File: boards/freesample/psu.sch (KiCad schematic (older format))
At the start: 0 parts

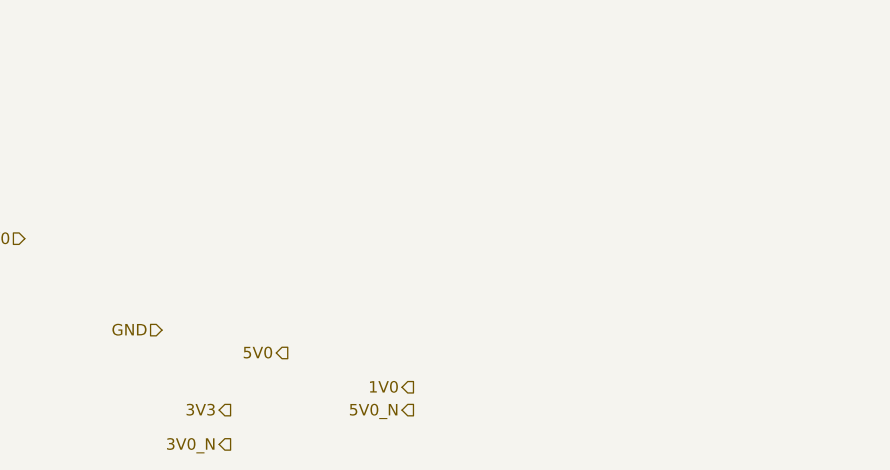
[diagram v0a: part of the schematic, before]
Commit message: Continued initial schematic capture
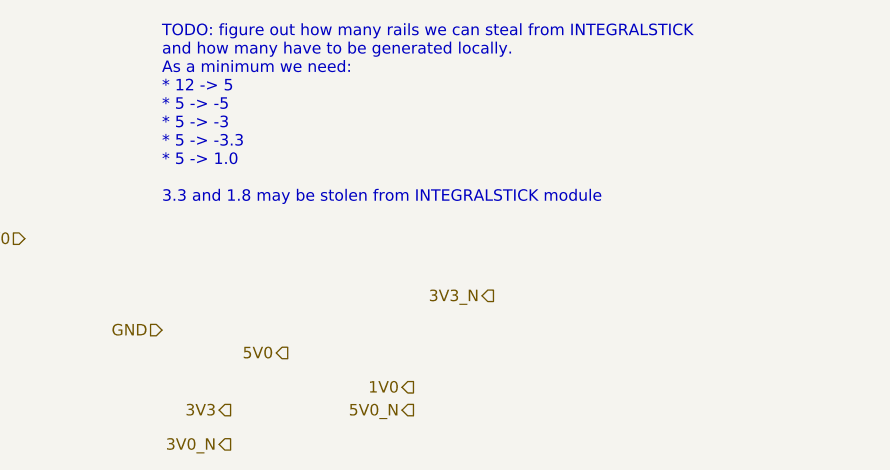
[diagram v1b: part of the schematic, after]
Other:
- note added: "TODO: figure out how many rails we can steal from INTEGRALSTICK\nand how many have to be generated locally.\nAs a minimum we need:\n* 12 -> 5\n* 5 -> -5\n* 5 -> -3\n* 5 -> -3.3\n* 5 -> 1.0\n\n3.3 and 1.8 may be stolen from INTEGRALSTICK module"
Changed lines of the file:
@@
 $Descr A4 11693 8268
 encoding utf-8
-Sheet 10 11
+Sheet 10 12
 Title "FREESAMPLE Oscilloscope"
-Date "2018-12-15"
+Date "2018-12-17"
 Rev "0.1"
 Comp "Andrew D. Zonenberg / Antikernel Labs"
@@
 Text HLabel 1100 1750 0    50   Input ~ 0
 12V0
+Text Notes 1700 1600 0    50   ~ 0
+TODO: figure out how many rails we can steal from INTEGRALSTICK\nand how many have to be generated locally.\nAs a minimum we need:\n* 12 -> 5\n* 5 -> -5\n* 5 -> -3\n* 5 -> -3.3\n* 5 -> 1.0\n\n3.3 and 1.8 may be stolen from INTEGRALSTICK module
+Text HLabel 3150 2000 0    50   Output ~ 0
+3V3_N
 $EndSCHEMATC

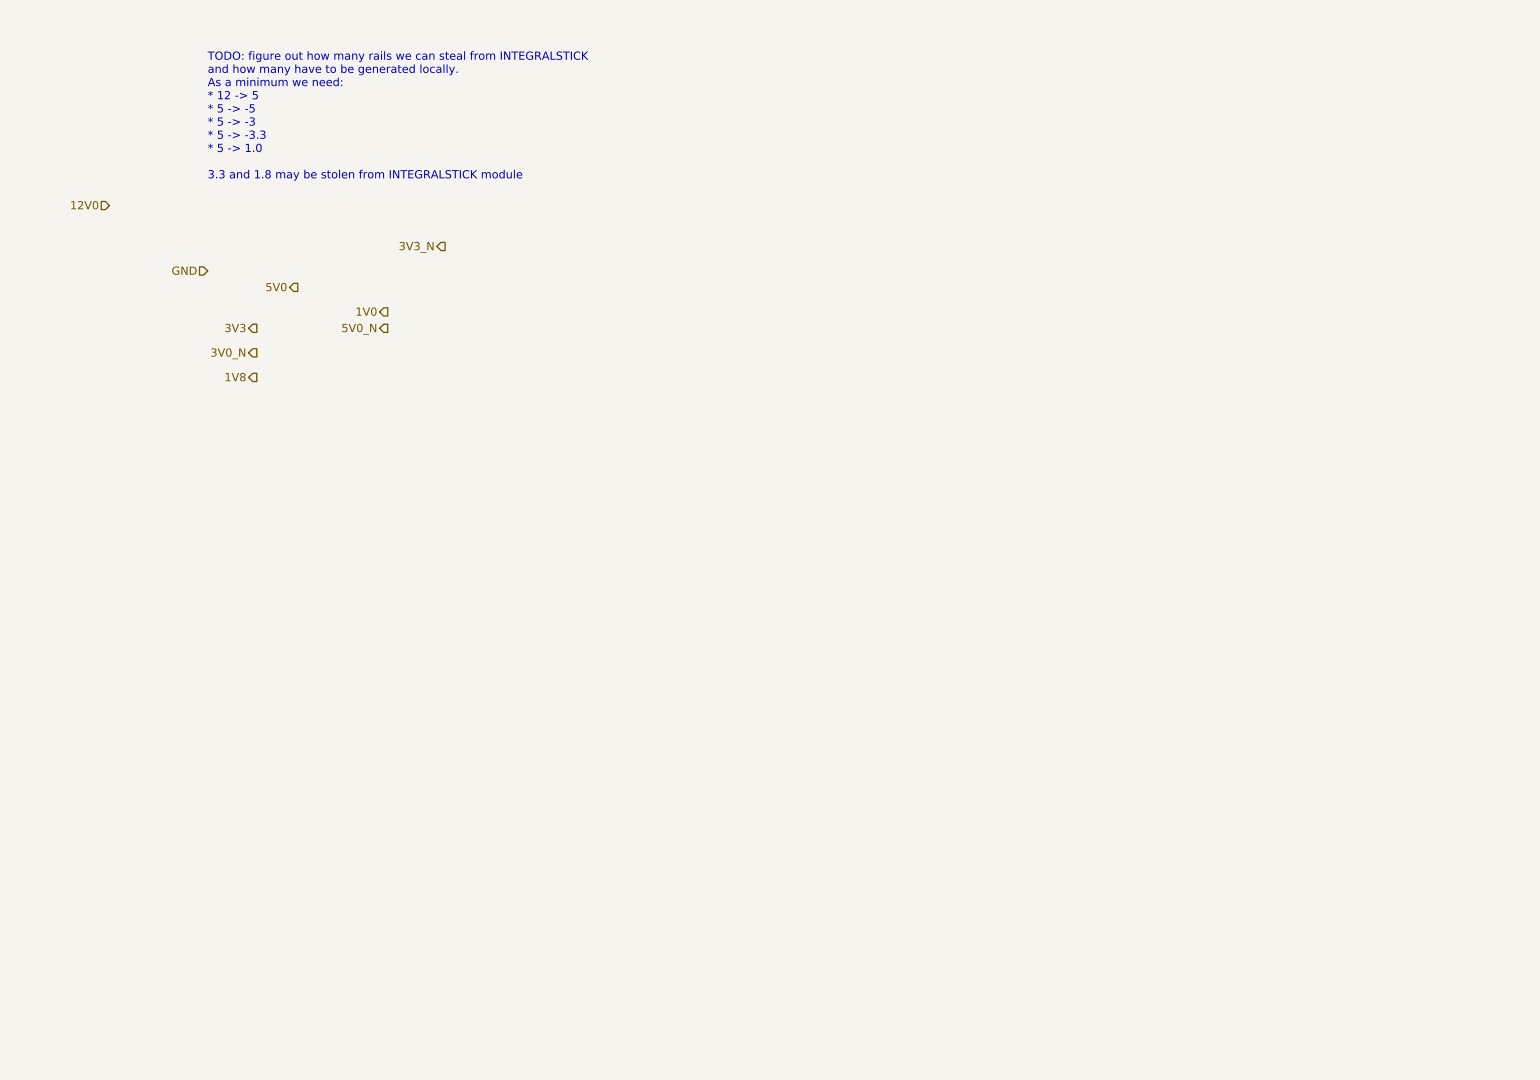
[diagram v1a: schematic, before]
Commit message: Continued work on FREESAMPLE schematic including PSU.
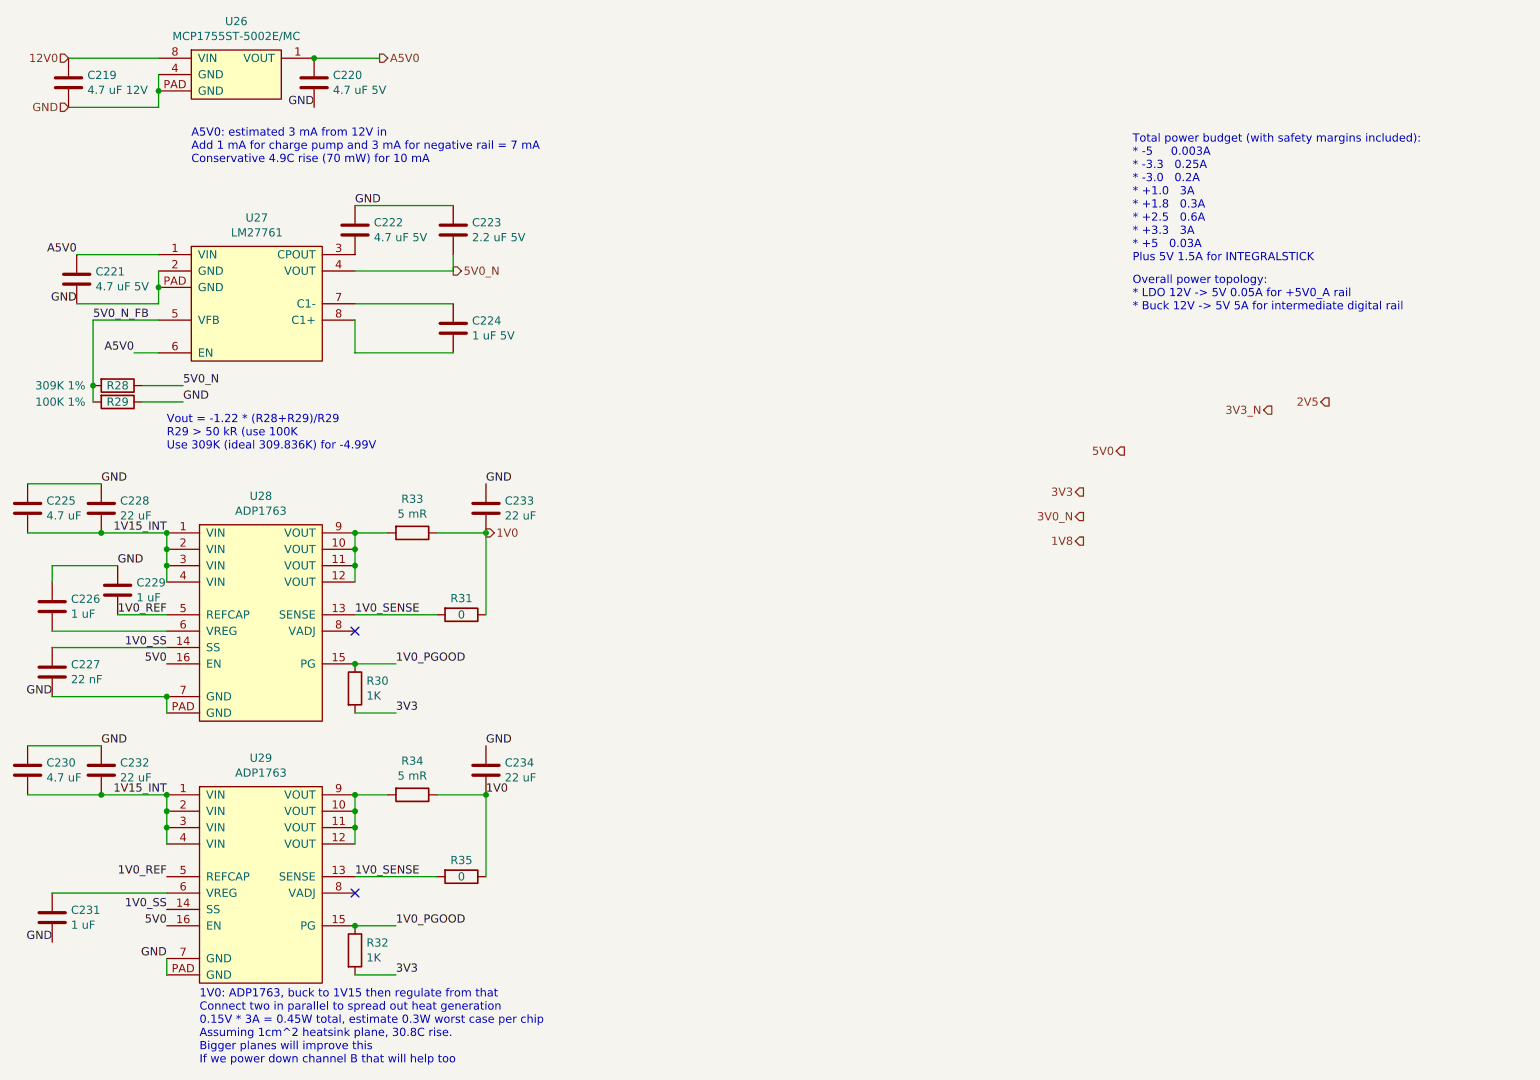
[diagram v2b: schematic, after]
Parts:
- added C219: 4.7 uF 12V, symbol device:C
- added C220, C221, C222: 4.7 uF 5V, symbol device:C
- added C223: 2.2 uF 5V, symbol device:C
- added C224: 1 uF 5V, symbol device:C
- added C225, C230: 4.7 uF, symbol device:C
- added C226, C229, C231: 1 uF, symbol device:C
- added C227: 22 nF, symbol device:C
- added C228, C232, C233, C234: 22 uF, symbol device:C
- added R28: 309K 1%, symbol device:R
- added R29: 100K 1%, symbol device:R
- added R30, R32: 1K, symbol device:R
- added R31, R35: 0, symbol device:R
- added R33, R34: 5 mR, symbol device:R
- added U26: MCP1755ST-5002E/MC, symbol power-azonenberg:MCP1755S-DFN
- added U27: LM27761, symbol power-azonenberg:LM27761
- added U28, U29: ADP1763, symbol power-azonenberg:ADP1763
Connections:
- net 12V0: now also C219.1, U26.8 (VIN)
- net 1V0: now also C233.1, C234.1, R31.1, R33.1, R34.1, R35.1
- net 3V3: now also R30.2, R32.2
- net 5V0: now also U28.16 (EN), U29.16 (EN)
- net 5V0_N: now also C223.2, R28.1, U27.4 (VOUT)
- net GND: now also C219.2, C220.2, C221.2, C222.1, C223.1, C225.2, C226.2, C227.1, C228.2, C229.2, C230.2, C231.1, C232.2, C233.2, C234.2, R29.1, U26.4 (GND), U26.PAD (GND), U27.2 (GND), U27.PAD (GND), U28.7 (GND), U28.PAD (GND), U29.7 (GND), U29.PAD (GND)
- new net: C222.2, U27.3 (CPOUT)
- new net: C224.1, U27.7 (C1-)
- new net: C224.2, U27.8 (C1+)
- new net: R33.2, U28.10 (VOUT), U28.11 (VOUT), U28.12 (VOUT), U28.9 (VOUT)
- new net: C226.1, U28.6 (VREG)
- new net: R34.2, U29.10 (VOUT), U29.11 (VOUT), U29.12 (VOUT), U29.9 (VOUT)
- new net: C231.2, U29.6 (VREG)
- new net 1V0_PGOOD: R30.1, R32.1, U28.15 (PG), U29.15 (PG)
- new net 1V0_REF: C229.1, U28.5 (REFCAP), U29.5 (REFCAP)
- new net 1V0_SENSE: R31.2, R35.2, U28.13 (SENSE), U29.13 (SENSE)
- new net 1V0_SS: C227.2, U28.14 (SS), U29.14 (SS)
- new net 1V15_INT: C225.1, C228.1, C230.1, C232.1, U28.1 (VIN), U28.2 (VIN), U28.3 (VIN), U28.4 (VIN), U29.1 (VIN), U29.2 (VIN), U29.3 (VIN), U29.4 (VIN)
- new net 5V0_N_FB: R28.2, R29.2, U27.5 (VFB)
- new net A5V0: C220.1, C221.1, U26.1 (VOUT), U27.1 (VIN), U27.6 (EN)
- no-connect marks 0 -> 2
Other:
- note added: "1V0: ADP1763, buck to 1V15 then regulate from that\nConnect two in parallel to spread out heat generation\n0.15V * 3A = 0.45W total, estimate 0.3W worst case per chip\nAssuming 1cm^2 heatsink plane, 30.8C rise.\nBigger planes will improve this\nIf we power down channel B that will help too"
- note added: "A5V0: estimated 3 mA from 12V in\nAdd 1 mA for charge pump and 3 mA for negative rail = 7 mA\nConservative 4.9C rise (70 mW) for 10 mA"
- note added: "Overall power topology:\n* LDO 12V -> 5V 0.05A for +5V0_A rail\n* Buck 12V -> 5V 5A for intermediate digital rail"
- note added: "Total power budget (with safety margins included):\n* -5 0.003A\n* -3.3 0.25A\n* -3.0 0.2A\n* +1.0 3A\n* +1.8 0.3A\n* +2.5 0.6A\n* +3.3 3A\n* +5 0.03A\nPlus 5V 1.5A for INTEGRALSTICK"
- note added: "Vout = -1.22 * (R28+R29)/R29\nR29 > 50 kR (use 100K\nUse 309K (ideal 309.836K) for -4.99V"
- note removed: "TODO: figure out how many rails we can steal from INTEGRALSTICK\nand how many have to be generated locally.\nAs a minimum we need:\n* 12 -> 5\n* 5 -> -5\n* 5 -> -3\n* 5 -> -3.3\n* 5 -> 1.0\n\n3.3 and 1.8 may be stolen from INTEGRALSTICK module"

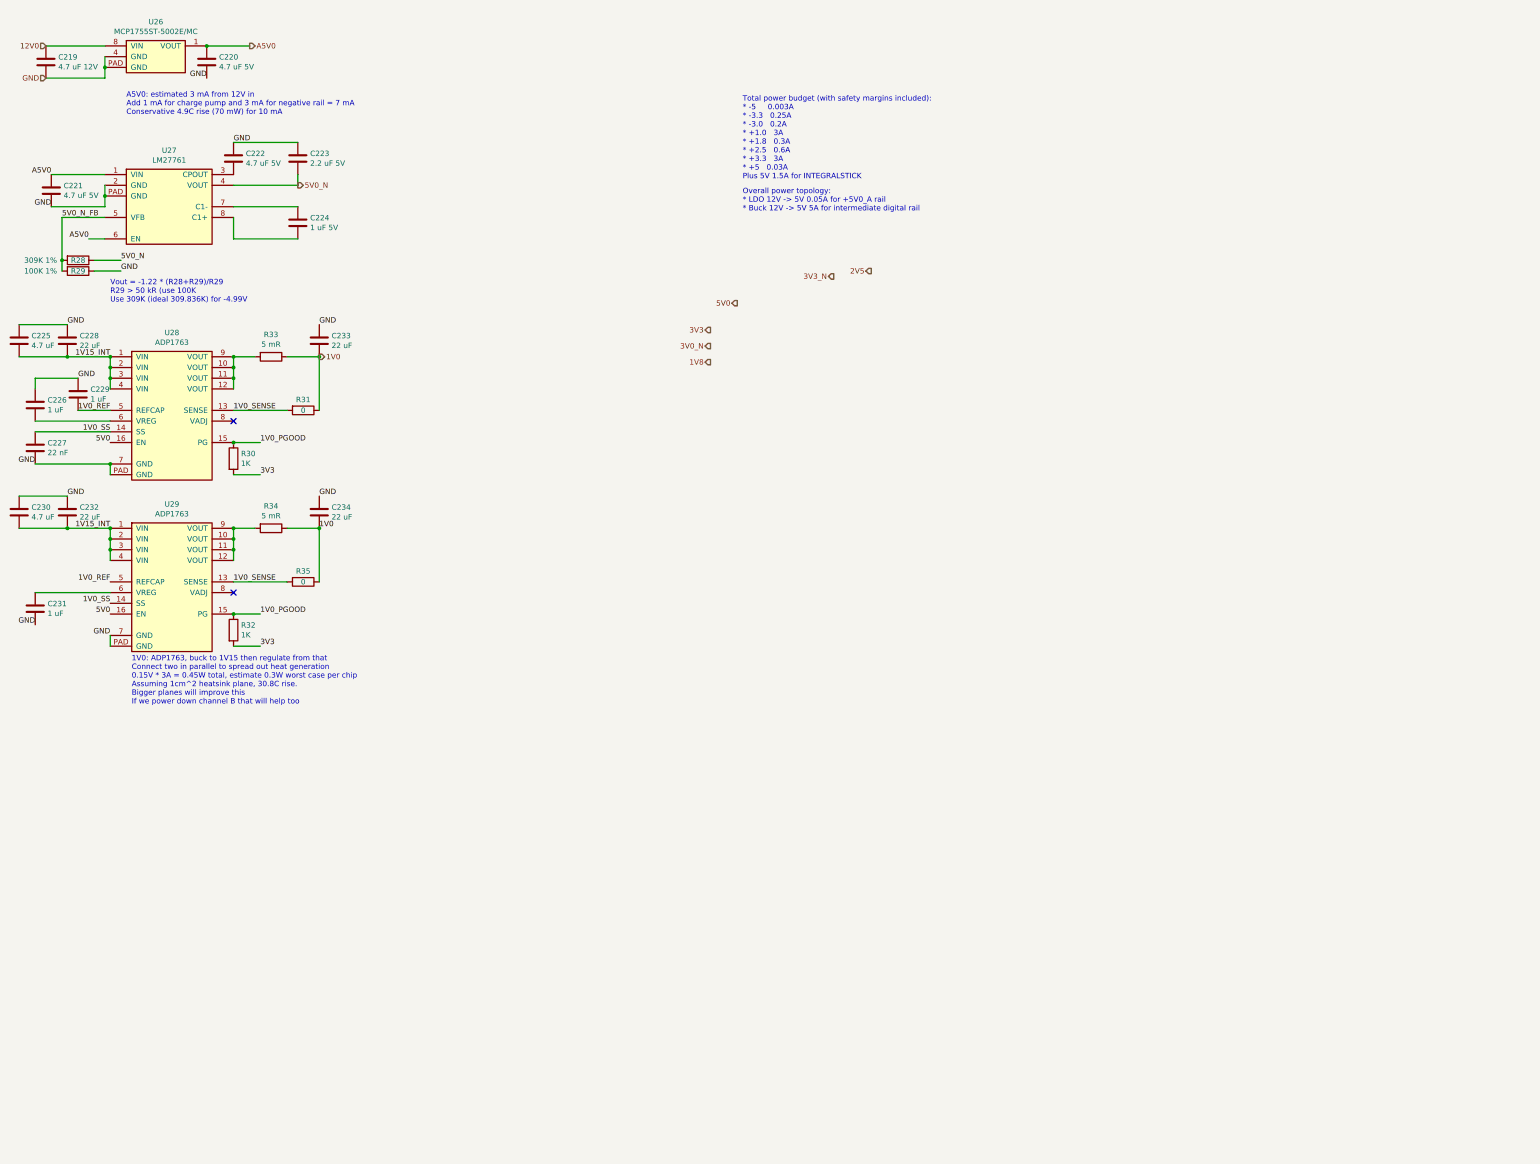
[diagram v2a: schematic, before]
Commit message: Lots more work on PSU and sch readability improvements
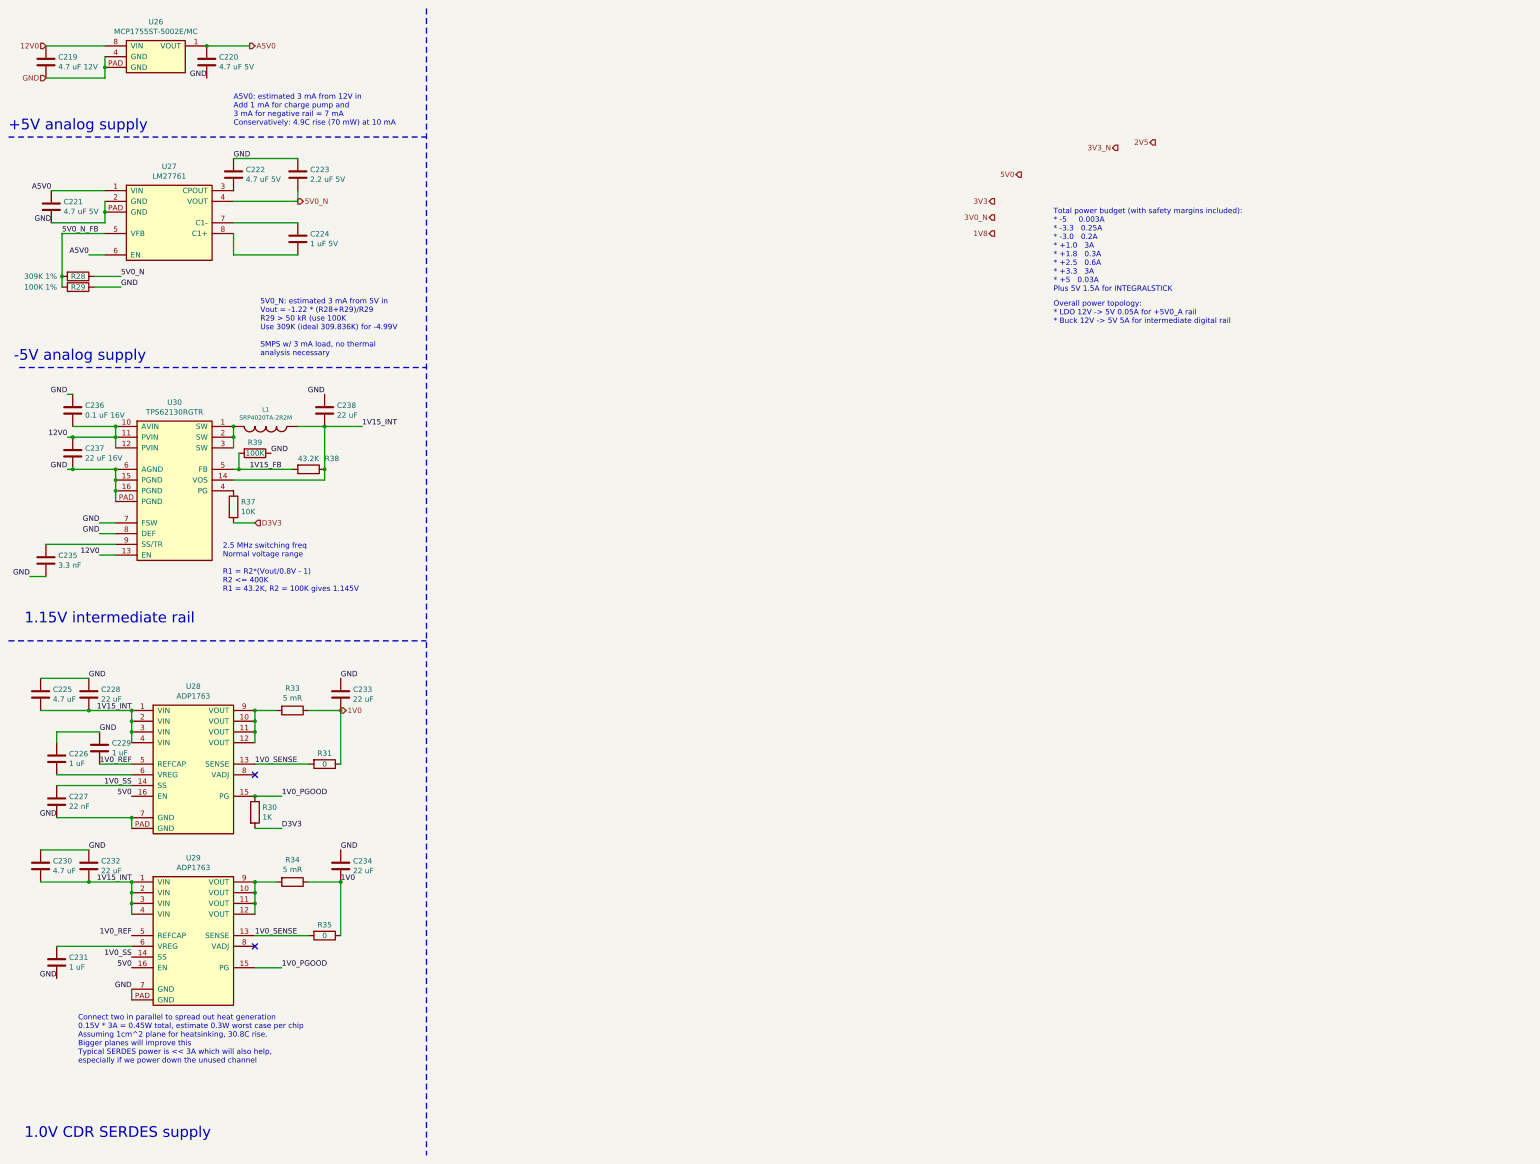
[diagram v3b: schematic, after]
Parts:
- removed R32: 1K, symbol device:R
- added C235: 3.3 nF, symbol device:C
- added C236: 0.1 uF 16V, symbol device:C
- added C237: 22 uF 16V, symbol device:C
- added C238: 22 uF, symbol device:C
- added L1: SRP4020TA-2R2M, symbol passive-azonenberg:INDUCTOR_PWROUT
- added R37: 10K, symbol device:R
- added R38: 43.2K, symbol device:R
- added R39: 100K, symbol device:R
- added U30: TPS62130RGTR, symbol power-azonenberg:TPS62130RGTR
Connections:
- net 12V0: now also C236.2, C237.1, U30.10 (AVIN), U30.11 (PVIN), U30.12 (PVIN), U30.13 (EN)
- net 1V15_INT: now also C238.2, L1.1, R38.1, U30.14 (VOS)
- net 3V3: no longer R30.2
- net GND: now also C235.2, C236.1, C237.2, C238.1, R39.1, U30.15 (PGND), U30.16 (PGND), U30.6 (AGND), U30.7 (FSW), U30.8 (DEF), U30.PAD (PGND)
- new net: L1.2, U30.1 (SW), U30.2 (SW), U30.3 (SW)
- new net: R37.1, U30.4 (PG)
- new net: C235.1, U30.9 (SS/TR)
- new net 1V15_FB: R38.2, R39.2, U30.5 (FB)
- new net D3V3: R30.2, R37.2
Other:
- note added: "+5V analog supply"
- note added: "-5V analog supply"
- note added: "1.0V CDR SERDES supply"
- note added: "1.15V intermediate rail"
- note added: "2.5 MHz switching freq\nNormal voltage range\n\nR1 = R2*(Vout/0.8V - 1)\nR2 <= 400K\nR1 = 43.2K, R2 = 100K gives 1.145V"
- note added: "5V0_N: estimated 3 mA from 5V in\nVout = -1.22 * (R28+R29)/R29\nR29 > 50 kR (use 100K\nUse 309K (ideal 309.836K) for -4.99V\n\nSMPS w/ 3 mA load, no thermal\nanalysis necessary"
- note added: "A5V0: estimated 3 mA from 12V in\nAdd 1 mA for charge pump and\n3 mA for negative rail = 7 mA\nConservatively: 4.9C rise (70 mW) at 10 mA"
- note added: "Connect two in parallel to spread out heat generation\n0.15V * 3A = 0.45W total, estimate 0.3W worst case per chip\nAssuming 1cm^2 plane for heatsinking, 30.8C rise.\nBigger planes will improve this\nTypical SERDES power is << 3A which will also help,\nespecially if we power down the unused channel"
- note removed: "1V0: ADP1763, buck to 1V15 then regulate from that\nConnect two in parallel to spread out heat generation\n0.15V * 3A = 0.45W total, estimate 0.3W worst case per chip\nAssuming 1cm^2 heatsink plane, 30.8C rise.\nBigger planes will improve this\nIf we power down channel B that will help too"
- note removed: "A5V0: estimated 3 mA from 12V in\nAdd 1 mA for charge pump and 3 mA for negative rail = 7 mA\nConservative 4.9C rise (70 mW) for 10 mA"
- note removed: "Vout = -1.22 * (R28+R29)/R29\nR29 > 50 kR (use 100K\nUse 309K (ideal 309.836K) for -4.99V"
- moved on the sheet: C221, C222, C223, C224, C225, C226, C227, C228, C229, C230, C231, C232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
